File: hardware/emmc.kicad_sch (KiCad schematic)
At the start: 25 parts, among them U7 EMMC16G-TB29-PZ90

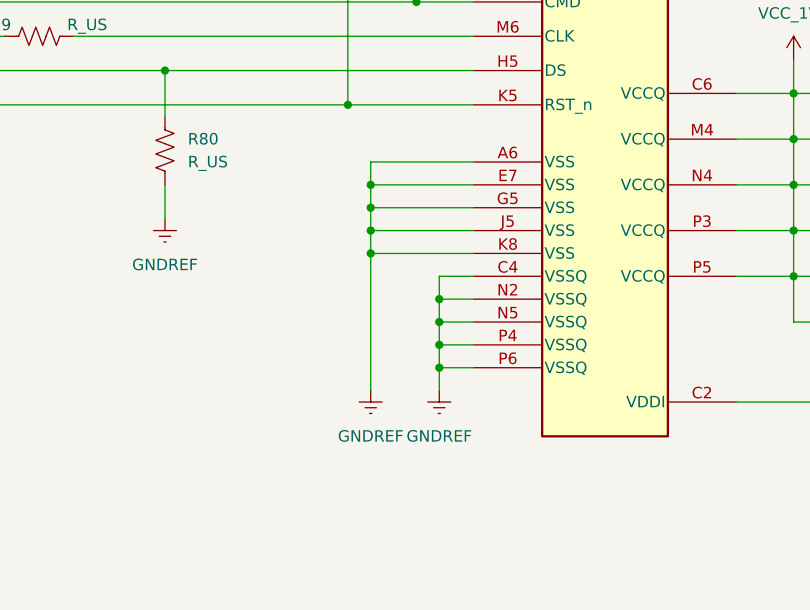
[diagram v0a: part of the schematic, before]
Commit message: update schematic
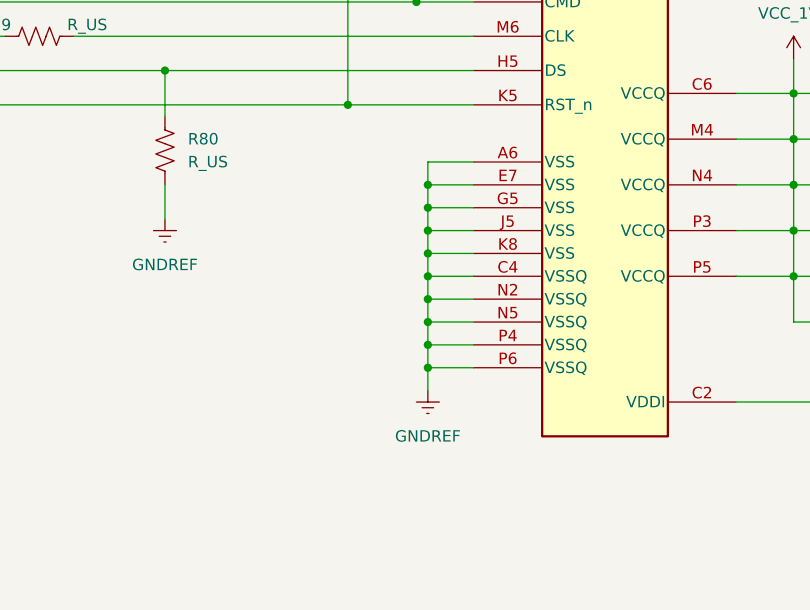
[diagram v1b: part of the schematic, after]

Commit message: updated schematic
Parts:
- added U9: MPFS025T-FCVG484E, MPFS250T/MPFS160T/MPFS095T/MPFS025T-FCVG484_MCH, symbol payload-sym:MPFS025T-FCVG484E
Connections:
- net EMMC_CLK: now also U9.J1 (MSSIO0B4)
- net EMMC_CMD: now also U9.K5 (MSSIO1B4)
- net EMMC_DATA0: now also U9.H1 (MSSIO2B4)
- net EMMC_DATA1: now also U9.J4 (MSSIO3B4)
- net EMMC_DATA2: now also U9.K4 (MSSIO4B4)
- net EMMC_DATA3: now also U9.J7 (MSSIO5B4)
- net EMMC_DATA4: now also U9.J6 (MSSIO8B4)
- net EMMC_DATA5: now also U9.H6 (MSSIO9B4)
- net EMMC_DATA6: now also U9.J3 (MSSIO10B4)
- net EMMC_DATA7: now also U9.H2 (MSSIO11B4)
- net EMMC_RSTn: now also U9.H4 (MSSIO7B4)
- new net EMMC_DQ: U9.K3 (MSSIO6B4)
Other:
- moved on the sheet: U7B

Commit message: need finish io banks pinouts
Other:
- note added: "eMMC FPGA BANK"
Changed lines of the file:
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@@
 	(generator_version "10.0")
 	(paper "A3")
+	(text "eMMC FPGA BANK"
+		(exclude_from_sim no)
+		(at 114.808 174.498 0)
+		(effects
+			(font
+				(size 3.81 3.81)
+				(thickness 1.016)
+				(bold yes)
+			)
+		)
+	)
 	(text "EMMC\n"
 		(exclude_from_sim no)
